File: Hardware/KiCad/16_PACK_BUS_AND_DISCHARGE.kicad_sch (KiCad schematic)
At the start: 0 parts

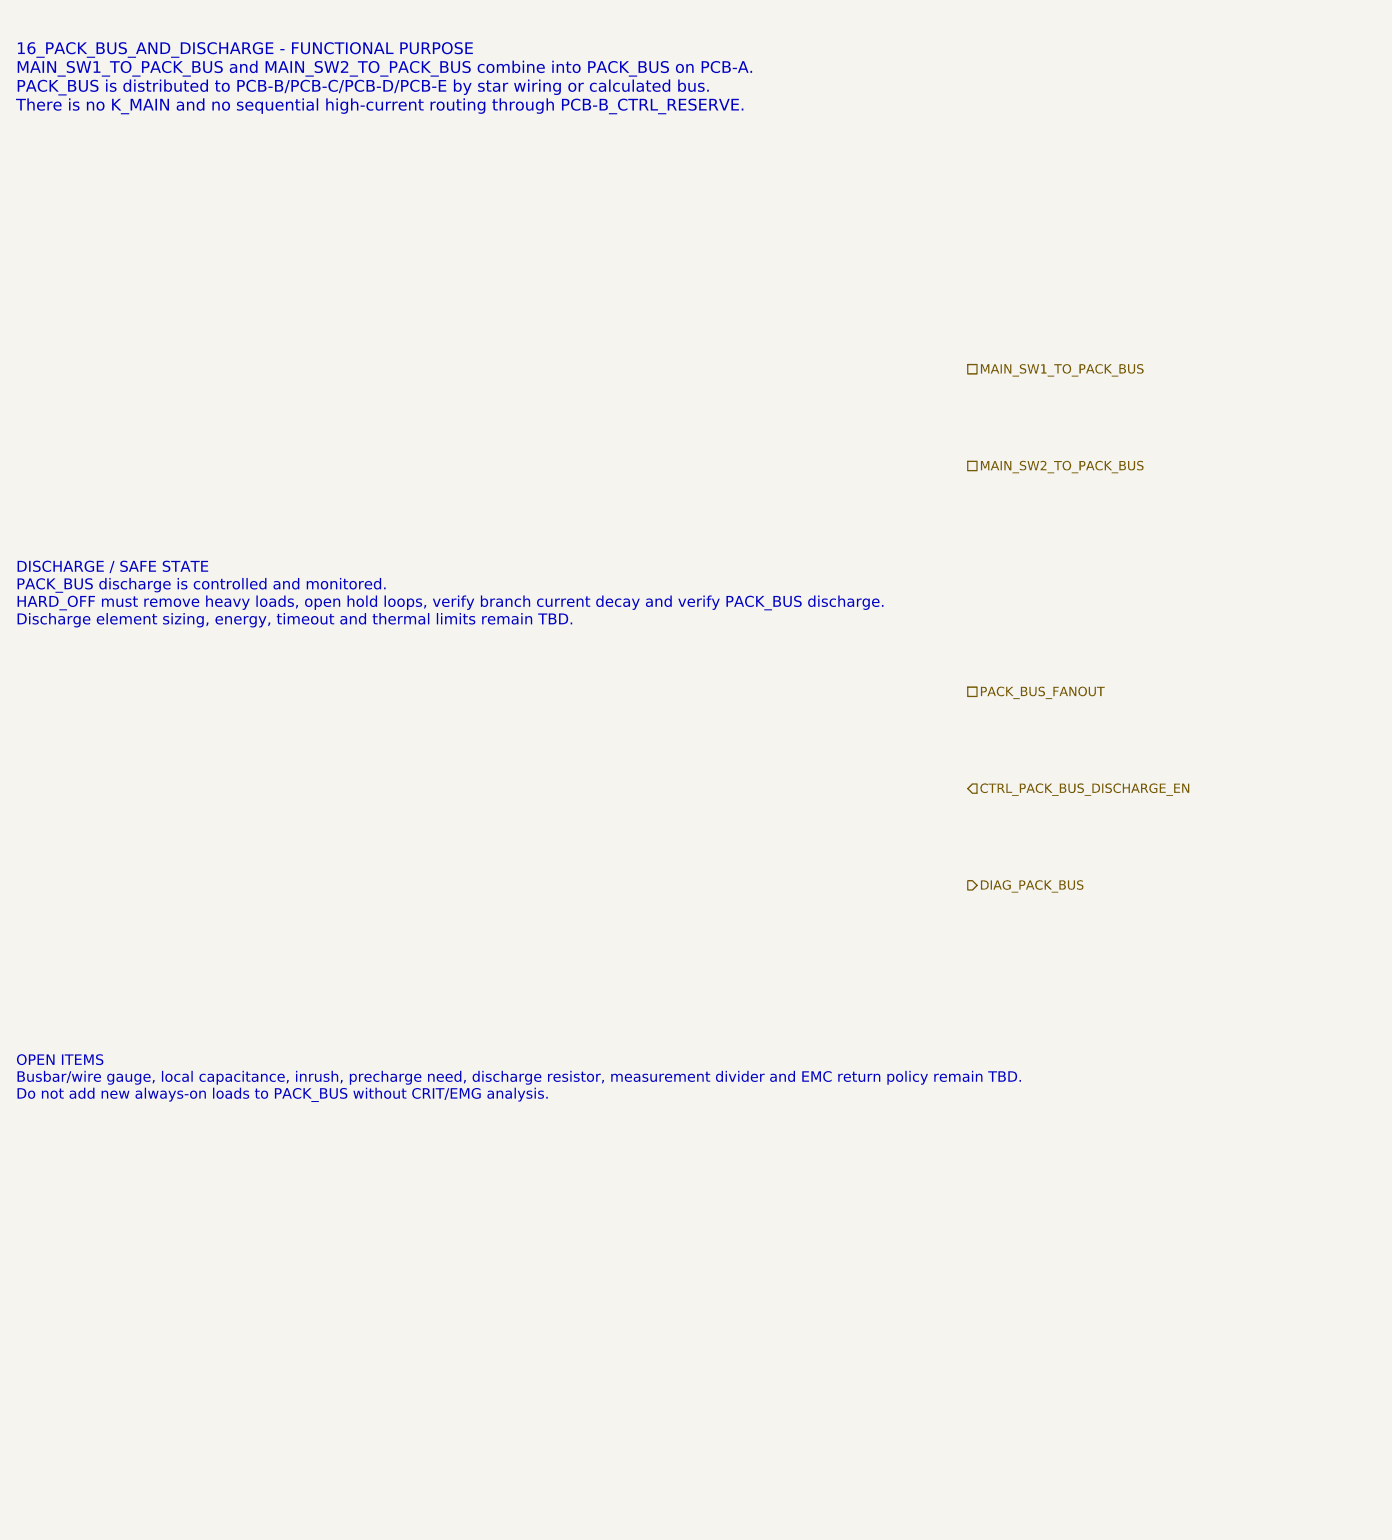
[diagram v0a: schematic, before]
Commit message: hardware: refine PACK_BUS and discharge level B
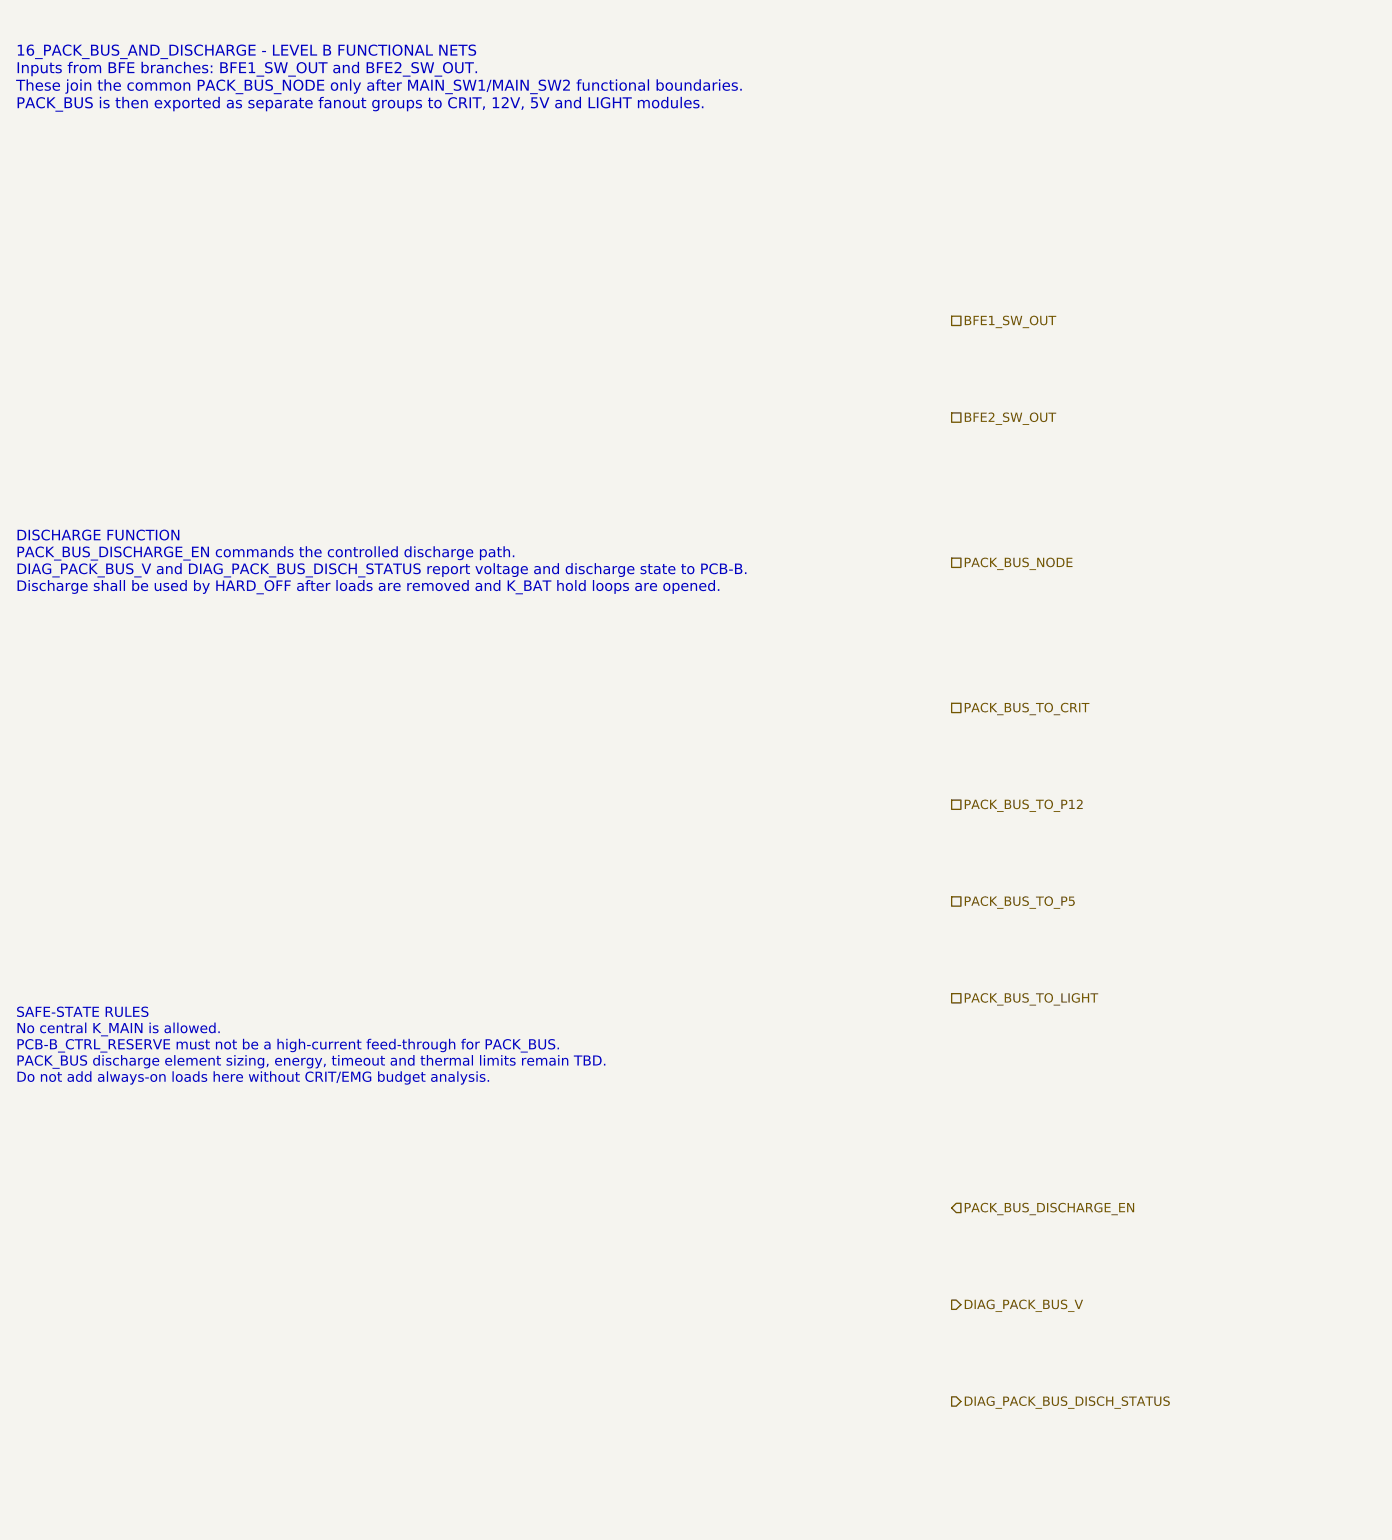
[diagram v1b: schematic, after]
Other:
- note added: "16_PACK_BUS_AND_DISCHARGE - LEVEL B FUNCTIONAL NETS Inputs from BFE branches: BFE1_SW_OUT and BFE2_SW_OUT. These join the common PACK_BUS_NODE only after MAIN_SW1/MAIN_SW2 functional boundaries. PACK_BUS is then exported as separate fanout groups to CRIT, 12V, 5V and LIGHT modules."
- note added: "DISCHARGE FUNCTION PACK_BUS_DISCHARGE_EN commands the controlled discharge path. DIAG_PACK_BUS_V and DIAG_PACK_BUS_DISCH_STATUS report voltage and discharge state to PCB-B. Discharge shall be used by HARD_OFF after loads are removed and K_BAT hold loops are opened."
- note added: "SAFE-STATE RULES No central K_MAIN is allowed. PCB-B_CTRL_RESERVE must not be a high-current feed-through for PACK_BUS. PACK_BUS discharge element sizing, energy, timeout and thermal limits remain TBD. Do not add always-on loads here without CRIT/EMG budget analysis."
- note removed: "16_PACK_BUS_AND_DISCHARGE - FUNCTIONAL PURPOSE MAIN_SW1_TO_PACK_BUS and MAIN_SW2_TO_PACK_BUS combine into PACK_BUS on PCB-A. PACK_BUS is distributed to PCB-B/PCB-C/PCB-D/PCB-E by star wiring or calculated bus. There is no K_MAIN and no sequential high-current routing through PCB-B_CTRL_RESERVE."
- note removed: "DISCHARGE / SAFE STATE PACK_BUS discharge is controlled and monitored. HARD_OFF must remove heavy loads, open hold loops, verify branch current decay and verify PACK_BUS discharge. Discharge element sizing, energy, timeout and thermal limits remain TBD."
- note removed: "OPEN ITEMS Busbar/wire gauge, local capacitance, inrush, precharge need, discharge resistor, measurement divider and EMC return policy remain TBD. Do not add new always-on loads to PACK_BUS without CRIT/EMG analysis."
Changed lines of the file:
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@@
 	(generator "eeschema")
 	(generator_version "10.0")
-	(uuid "bfe-dh-00000016-0000-4000-8000-000000000016")
+	(uuid "bfe-lb-00000016-0000-4000-8000-000000000016")
 	(paper "A3")
 	(title_block
 		(title "16_PACK_BUS_AND_DISCHARGE - PACK_BUS creation")
 		(date "2026-07-15")
-		(rev "A1")
+		(rev "B1")
 		(company "Gonoboben/plataVM")
-		(comment 1 "Architecture Level A: PACK_BUS fanout and discharge boundary")
-		(comment 2 "No central K_MAIN and no PCB-B high-current feed-through")
+		(comment 1 "Architecture Level B: PACK_BUS net groups and discharge logic")
+		(comment 2 "No K_MAIN, no discharge component values, no busbar/wire gauge selected")
 	)
-	(text "16_PACK_BUS_AND_DISCHARGE - FUNCTIONAL PURPOSE\nMAIN_SW1_TO_PACK_BUS and MAIN_SW2_TO_PACK_BUS combine into PACK_BUS on PCB-A.\nPACK_BUS is distributed to PCB-B/PCB-C/PCB-D/PCB-E by star wiring or calculated bus.\nThere is no K_MAIN and no sequential high-current routing through PCB-B_CTRL_RESERVE."
+	(text "16_PACK_BUS_AND_DISCHARGE - LEVEL B FUNCTIONAL NETS\nInputs from BFE branches: BFE1_SW_OUT and BFE2_SW_OUT.\nThese join the common PACK_BUS_NODE only after MAIN_SW1/MAIN_SW2 functional boundaries.\nPACK_BUS is then exported as separate fanout groups to CRIT, 12V, 5V and LIGHT modules."
 		(exclude_from_sim no)
 		(at 12 18 0)
-		(effects (font (size 1.45 1.45)) (justify left))
-		(uuid "bfe-dh-00000016-0000-4000-8000-000000000101")
+		(effects (font (size 1.35 1.35)) (justify left))
+		(uuid "bfe-lb-00000016-0000-4000-8000-000000000101")
 	)
-	(text "DISCHARGE / SAFE STATE\nPACK_BUS discharge is controlled and monitored.\nHARD_OFF must remove heavy loads, open hold loops, verify branch current decay and verify PACK_BUS discharge.\nDischarge element sizing, energy, timeout and thermal limits remain TBD."
+	(text "DISCHARGE FUNCTION\nPACK_BUS_DISCHARGE_EN commands the controlled discharge path.\nDIAG_PACK_BUS_V and DIAG_PACK_BUS_DISCH_STATUS report voltage and discharge state to PCB-B.\nDischarge shall be used by HARD_OFF after loads are removed and K_BAT hold loops are opened."
 		(exclude_from_sim no)
-		(at 12 82 0)
-		(effects (font (size 1.35 1.35)) (justify left))
-		(uuid "bfe-dh-00000016-0000-4000-8000-000000000102")
+		(at 12 78 0)
+		(effects (font (size 1.3 1.3)) (justify left))
+		(uuid "bfe-lb-00000016-0000-4000-8000-000000000102")
 	)
-	(text "OPEN ITEMS\nBusbar/wire gauge, local capacitance, inrush, precharge need, discharge resistor, measurement divider and EMC return policy remain TBD.\nDo not add new always-on loads to PACK_BUS without CRIT/EMG analysis."
+	(text "SAFE-STATE RULES\nNo central K_MAIN is allowed.\nPCB-B_CTRL_RESERVE must not be a high-current feed-through for PACK_BUS.\nPACK_BUS discharge element sizing, energy, timeout and thermal limits remain TBD.\nDo not add always-on loads here without CRIT/EMG budget analysis."
 		(exclude_from_sim no)
-		(at 12 142 0)
-		(effects (font (size 1.3 1.3)) (justify left))
-		(uuid "bfe-dh-00000016-0000-4000-8000-000000000103")
+		(at 12 138 0)
+		(effects (font (size 1.25 1.25)) (justify left))
+		(uuid "bfe-lb-00000016-0000-4000-8000-000000000103")
 	)
-	(hierarchical_label "MAIN_SW1_TO_PACK_BUS" (shape passive) (exclude_from_sim no) (at 130 54 0) (effects (font (size 1.15 1.15)) (justify left)) (uuid "bfe-dh-00000016-0000-4000-8000-000000000201"))
-	(hierarchical_label "MAIN_SW2_TO_PACK_BUS" (shape passive) (exclude_from_sim no) (at 130 66 0) (effects (font (size 1.15 1.15)) (justify left)) (uuid "bfe-dh-00000016-0000-4000-8000-000000000202"))
-	(hierarchical_label "PACK_BUS_FANOUT" (shape passive) (exclude_from_sim no) (at 130 94 0) (effects (font (size 1.15 1.15)) (justify left)) (uuid "bfe-dh-00000016-0000-4000-8000-000000000203"))
-	(hierarchical_label "CTRL_PACK_BUS_DISCHARGE_EN" (shape input) (exclude_from_sim no) (at 130 106 0) (effects (font (size 1.15 1.15)) (justify left)) (uuid "bfe-dh-00000016-0000-4000-8000-000000000204"))
-	(hierarchical_label "DIAG_PACK_BUS" (shape output) (exclude_from_sim no) (at 130 118 0) (effects (font (size 1.15 1.15)) (justify left)) (uuid "bfe-dh-00000016-0000-4000-8000-000000000205"))
+	(hierarchical_label "BFE1_SW_OUT" (shape passive) (exclude_from_sim no) (at 128 48 0) (effects (font (size 1.15 1.15)) (justify left)) (uuid "bfe-lb-00000016-0000-4000-8000-000000000201"))
+	(hierarchical_label "BFE2_SW_OUT" (shape passive) (exclude_from_sim no) (at 128 60 0) (effects (font (size 1.15 1.15)) (justify left)) (uuid "bfe-lb-00000016-0000-4000-8000-000000000202"))
+	(hierarchical_label "PACK_BUS_NODE" (shape passive) (exclude_from_sim no) (at 128 78 0) (effects (font (size 1.15 1.15)) (justify left)) (uuid "bfe-lb-00000016-0000-4000-8000-000000000203"))
+	(hierarchical_label "PACK_BUS_TO_CRIT" (shape passive) (exclude_from_sim no) (at 128 96 0) (effects (font (size 1.15 1.15)) (justify left)) (uuid "bfe-lb-00000016-0000-4000-8000-000000000204"))
+	(hierarchical_label "PACK_BUS_TO_P12" (shape passive) (exclude_from_sim no) (at 128 108 0) (effects (font (size 1.15 1.15)) (justify left)) (uuid "bfe-lb-00000016-0000-4000-8000-000000000205"))
+	(hierarchical_label "PACK_BUS_TO_P5" (shape passive) (exclude_from_sim no) (at 128 120 0) (effects (font (size 1.15 1.15)) (justify left)) (uuid "bfe-lb-00000016-0000-4000-8000-000000000206"))
+	(hierarchical_label "PACK_BUS_TO_LIGHT" (shape passive) (exclude_from_sim no) (at 128 132 0) (effects (font (size 1.15 1.15)) (justify left)) (uuid "bfe-lb-00000016-0000-4000-8000-000000000207"))
+	(hierarchical_label "PACK_BUS_DISCHARGE_EN" (shape input) (exclude_from_sim no) (at 128 158 0) (effects (font (size 1.15 1.15)) (justify left)) (uuid "bfe-lb-00000016-0000-4000-8000-000000000208"))
+	(hierarchical_label "DIAG_PACK_BUS_V" (shape output) (exclude_from_sim no) (at 128 170 0) (effects (font (size 1.15 1.15)) (justify left)) (uuid "bfe-lb-00000016-0000-4000-8000-000000000209"))
+	(hierarchical_label "DIAG_PACK_BUS_DISCH_STATUS" (shape output) (exclude_from_sim no) (at 128 182 0) (effects (font (size 1.15 1.15)) (justify left)) (uuid "bfe-lb-00000016-0000-4000-8000-000000000210"))
 )
